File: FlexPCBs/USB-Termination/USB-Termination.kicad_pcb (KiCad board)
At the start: 2 copper layers, 26.9 x 10.3 mm, 31 parts, among them J1 Conn_01x08_Pin

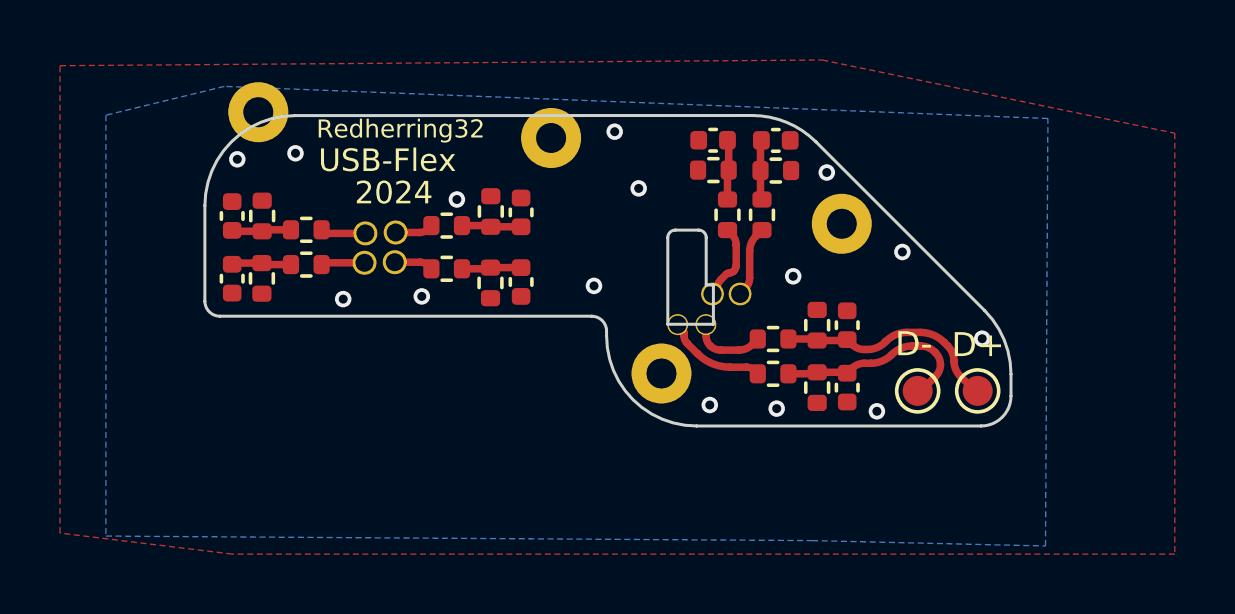
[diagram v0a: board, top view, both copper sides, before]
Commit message: Delete HDMI Flipper Design Add HDMI Flex Add USB C/Power and volume button PCB Add Housing CAD Update IDE Flex Update S Controller PCBs Update LPC Flex Update USB Flex
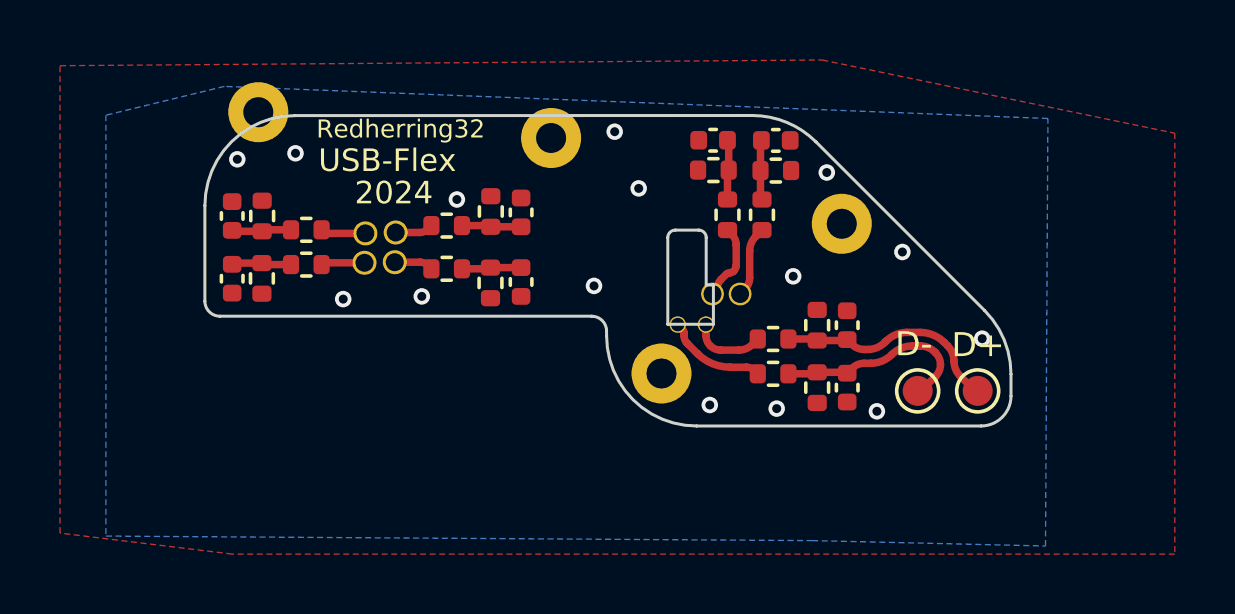
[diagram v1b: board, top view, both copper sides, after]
